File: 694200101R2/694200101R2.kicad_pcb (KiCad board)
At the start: 2 copper layers, 438.6 x 125.8 mm, 402 parts, among them J1 USB4085-GF-A, J2 Conn_01x05_Male, J3 Conn_01x02_Male, SW1 MX_SW, SW10 MX_SW, SW100 MX_SW, SW101 MX_SW, SW102 MX_SW, SW103 MX_SW, SW104 MX_SW, SW105 MX_SW, SW106 MX_SW, SW107 MX_SW, SW11 MX_SW, SW12 MX_SW, SW13 MX_SW, SW14 MX_SW, SW15 MX_SW, SW16 MX_SW, SW17 MX_SW, SW18 MX_SW, SW19 MX_SW, SW2 MX_SW, SW20 MX_SW, SW21 MX_SW, SW22 MX_SW, SW23 MX_SW, SW24 MX_SW, SW25 MX_SW, SW26 MX_SW, SW27 MX_SW, SW28 MX_SW, SW29 MX_SW, SW3 MX_SW, SW30 MX_SW, SW31 MX_SW, SW32 MX_SW, SW33 MX_SW, SW34 MX_SW, SW35 MX_SW, SW36 MX_SW, SW37 MX_SW, SW38 MX_SW, SW39 MX_SW, SW4 MX_SW, SW40 MX_SW, SW41 MX_SW, SW42 MX_SW, SW43 MX_SW, SW44 MX_SW, SW45 MX_SW, SW46 MX_SW, SW47 MX_SW, SW48 MX_SW, SW49 MX_SW, SW5 MX_SW, SW50 MX_SW, SW51 MX_SW, SW52 MX_SW, SW53 MX_SW, SW54 MX_SW, SW55 MX_SW, SW56 MX_SW, SW57 MX_SW, SW58 MX_SW, SW59 MX_SW, SW6 MX_SW, SW60 MX_SW, SW61 MX_SW, SW62 MX_SW, SW63 MX_SW, SW64 MX_SW, SW65 MX_SW, SW66 MX_SW, SW67 MX_SW, SW68 MX_SW, SW69 MX_SW, SW7 MX_SW, SW70 MX_SW, SW71 MX_SW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

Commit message: adjusted led and added pull on program
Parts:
- added R23: RNCP0603FTD10K0, Resistor-Libs:RESC1508X50N, F.Cu at (353.7, 20.6)
- J2: value Conn_01x05_Male -> Conn_01x06_Male; footprint Connector_PinHeader_2.54mm:PinHeader_1x05_P2.54mm_Vertical -> Connector_PinHeader_2.54mm:PinHeader_1x06_P2.54mm_Vertical
- R12, R14: value RNCP0603FTD10K0 -> MCT06030Z0000ZP500; footprint Resistor-Libs:RESC1508X50N -> Resistor-Libs:RESC1508X55N
- moved J2 2.44 mm to (308.5, 29.6)
- moved D217 1.38 mm to (301.3, 72.2)
- turned R12 to 90 degrees
- turned R14 to 90 degrees
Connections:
- J1 pad A8: (no net) -> Net-(J1-PadA8)
- J1 pad B8: (no net) -> Net-(J1-PadB8)
- R12 pad 1: Net-(ENC1-PadA1) -> ENCODER_A
- R12 pad 2: ENCODER_A -> Net-(ENC1-PadA1)
- R14 pad 1: Net-(ENC1-PadB1) -> ENCODER_B
- R14 pad 2: ENCODER_B -> Net-(ENC1-PadB1)
- U3 pad 10: (no net) -> COL_18
- U3 pad 14: (no net) -> Net-(U3-Pad14)
- U3 pad 15: (no net) -> Net-(U3-Pad15)
- U3 pad 16: (no net) -> Net-(U3-Pad16)
- U3 pad 17: (no net) -> Net-(U3-Pad17)
- U3 pad 2: (no net) -> Net-(U3-Pad2)
- U3 pad 3: (no net) -> Net-(U3-Pad3)
- U3 pad 4: (no net) -> Net-(U3-Pad4)
- U3 pad 56: (no net) -> ROW_1
- U3 pad 61: (no net) -> Net-(U3-Pad61)
- U3 pad 62: (no net) -> Net-(U3-Pad62)
- U3 pad 8: (no net) -> Net-(U3-Pad8)
- U5 pad 1: (no net) -> Net-(U5-Pad1)
- U5 pad 36: (no net) -> Net-(U5-Pad36)
- U5 pad 45: (no net) -> Net-(U5-Pad45)
- U6 pad 1: (no net) -> Net-(U6-Pad1)
- U6 pad 30: (no net) -> CS13_B
- U6 pad 31: (no net) -> CS14_B
- U6 pad 32: (no net) -> CS15_B
- U6 pad 33: (no net) -> CS16_B
- U6 pad 36: (no net) -> Net-(U6-Pad36)
- U6 pad 45: (no net) -> Net-(U6-Pad45)
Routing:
- net +3V3: track 803.5 -> 815.8 mm, vias 14 -> 15
- net Net-(J3-Pad2): track 2.42 -> 5.78 mm
- net SWO: track 33.6 -> 36.1 mm
- net SWCLK: track 44.4 -> 46.9 mm
- net /RST: track 49.9 -> 52.3 mm
- net SWDIO: track 40.8 -> 43.0 mm
- net GND: track 626.5 -> 628.8 mm
- net CS12_B: track 252.9 -> 254.3 mm
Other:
- board text added: "694200101R2"
- board text removed: "694200101R1"

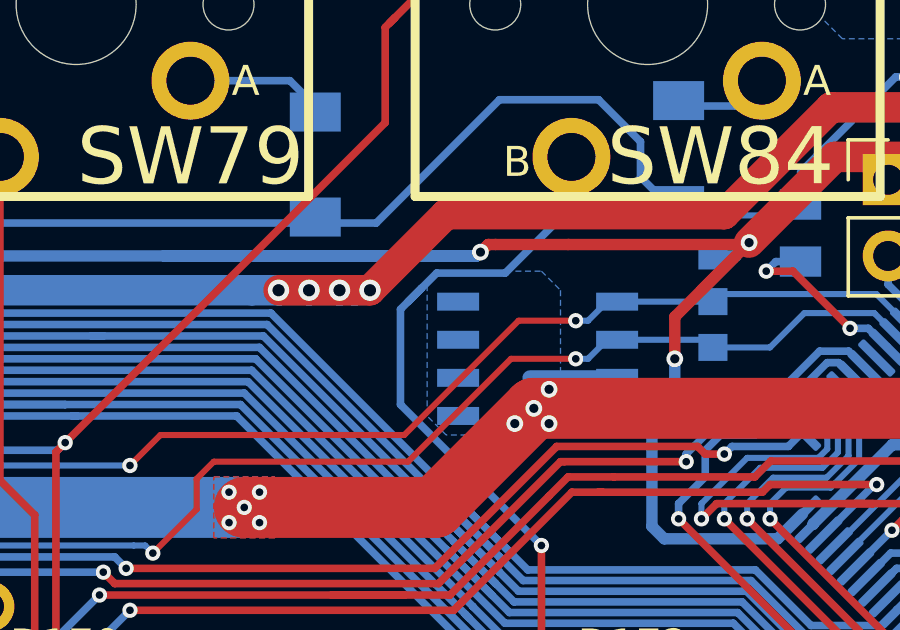
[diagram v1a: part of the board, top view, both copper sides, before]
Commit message: updated eeprom address
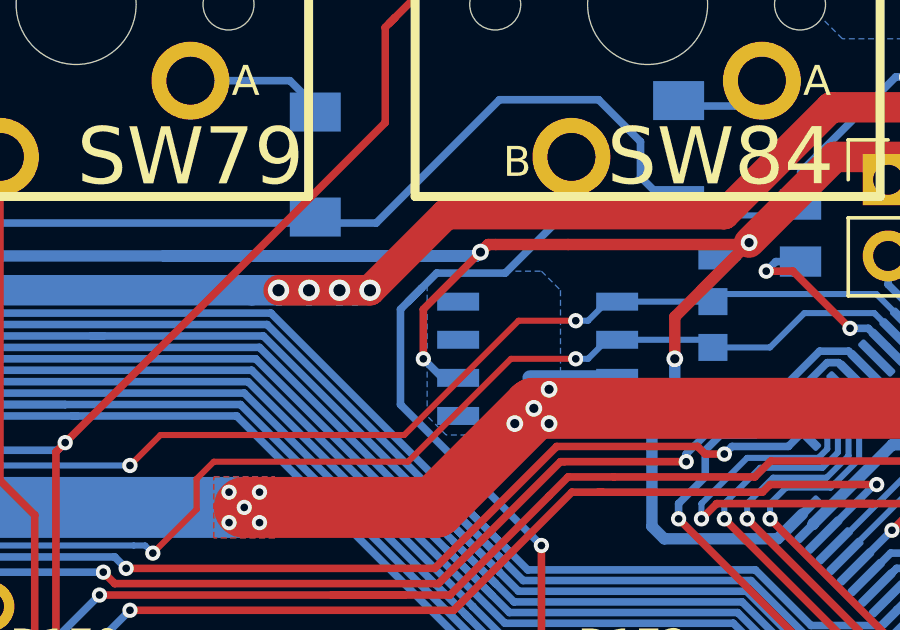
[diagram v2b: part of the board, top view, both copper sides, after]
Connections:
- U4 pad 2: GND -> +3V3
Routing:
- net +3V3: track 815.8 -> 821.5 mm, vias 15 -> 16

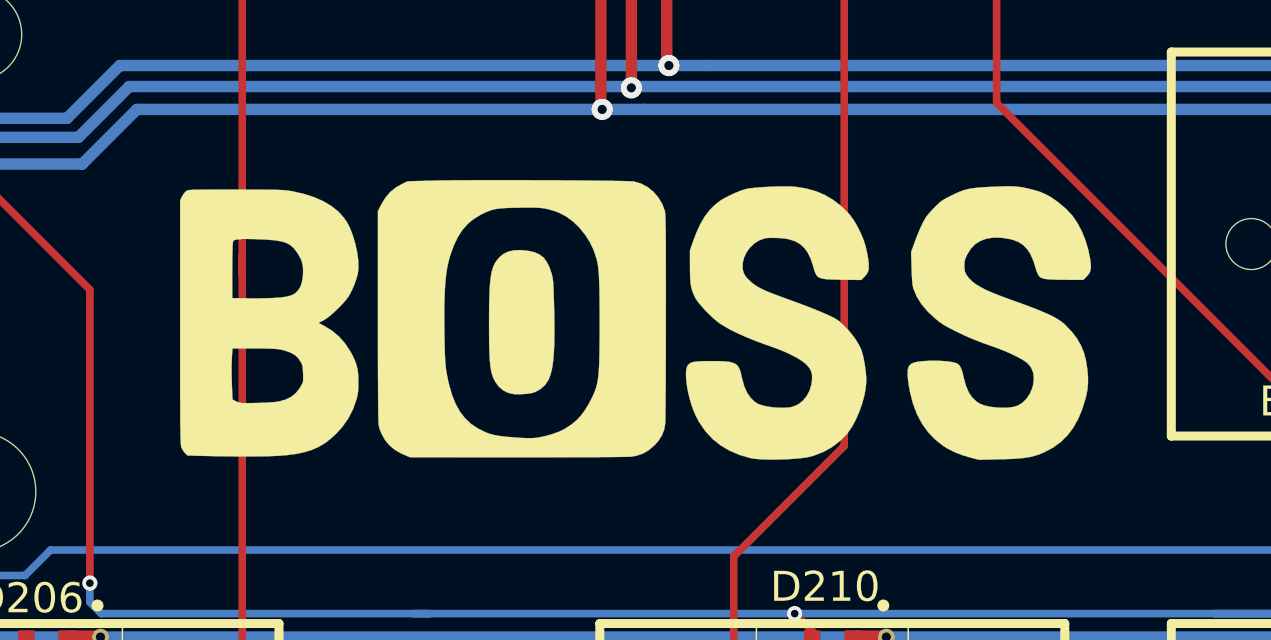
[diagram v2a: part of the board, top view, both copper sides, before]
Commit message: Added Logo and updated USB Connector
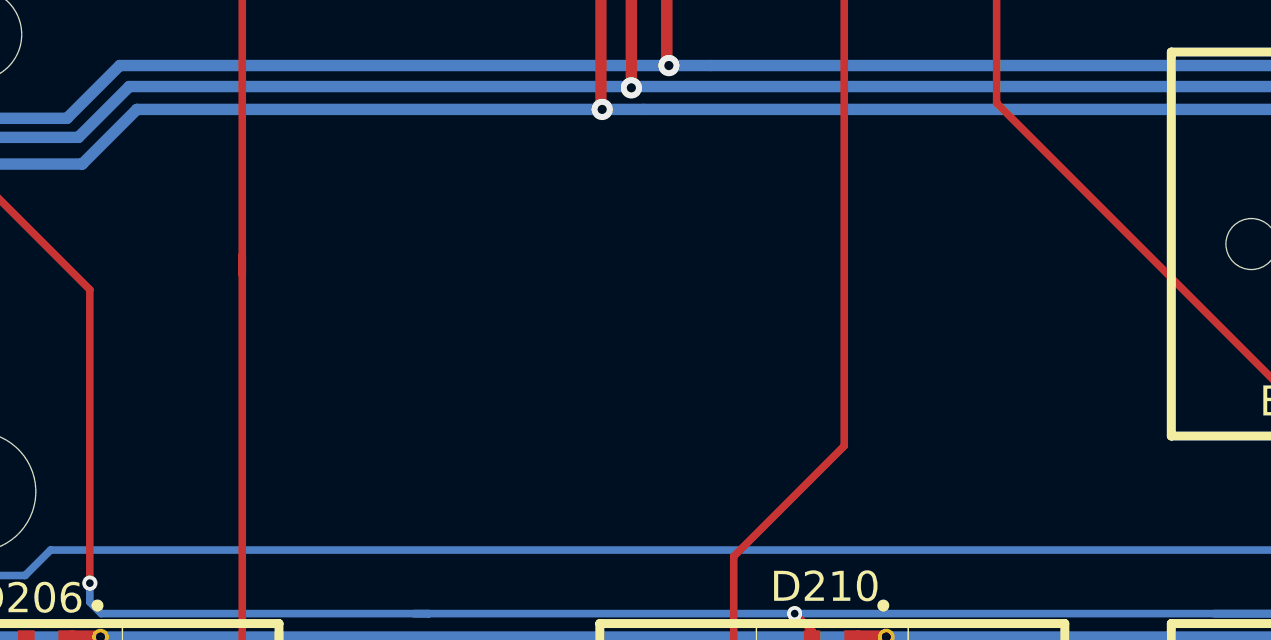
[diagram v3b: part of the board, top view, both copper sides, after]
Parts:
- removed G1: LOGO, BossLogo:BossLogo
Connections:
- U3 pad 10: COL_18 -> (no net)
- U3 pad 14: Net-(U3-Pad14) -> (no net)
- U3 pad 15: Net-(U3-Pad15) -> (no net)
- U3 pad 16: Net-(U3-Pad16) -> (no net)
- U3 pad 17: Net-(U3-Pad17) -> (no net)
- U3 pad 2: Net-(U3-Pad2) -> (no net)
- U3 pad 3: Net-(U3-Pad3) -> (no net)
- U3 pad 4: Net-(U3-Pad4) -> (no net)
- U3 pad 56: ROW_1 -> (no net)
- U3 pad 61: Net-(U3-Pad61) -> (no net)
- U3 pad 62: Net-(U3-Pad62) -> (no net)
- U3 pad 8: Net-(U3-Pad8) -> (no net)

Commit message: Prettied up schematic
Updated Schematic to be more readable and not as crazily wired
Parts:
- J1: value USB4085-GF-A -> USB_C_Receptacle_USB2.0; moved to F.Cu
- U5, U6: footprint cldg:QFN-48_EP_6.6x6.6_Pitch0.4mm -> Package_QFP:TQFP-48-1EP_7x7mm_P0.5mm_EP5x5mm_ThermalVias
- moved J1 9.96 mm to (358.1, -1.91), turned to 180 degrees
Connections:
- net /RST renamed RST
- net Net-(C3-Pad1) renamed OSC_OUT
- net Net-(C6-Pad1) renamed OSC_IN
- net Net-(J3-Pad2) renamed BOOT0
- net Net-(R3-Pad2) renamed ROW_3_MCU
- net Net-(R4-Pad2) renamed ROW_2_MCU
- net Net-(R5-Pad2) renamed ROW_6_MCU
- net Net-(R6-Pad2) renamed ROW_5_MCU
- net Net-(R7-Pad2) renamed ROW_4_MCU
- net Net-(R8-Pad1) renamed ROW_0_MCU
- J1 pad A8: Net-(J1-PadA8) -> (no net)
- J1 pad B8: Net-(J1-PadB8) -> (no net)
- J1 pad S1: (no net) -> Earth
- U5 pad 1: Net-(U5-Pad1) -> (no net)
- U5 pad 36: Net-(U5-Pad36) -> (no net)
- U5 pad 45: Net-(U5-Pad45) -> (no net)
- U6 pad 1: Net-(U6-Pad1) -> (no net)
- U6 pad 30: CS13_B -> (no net)
- U6 pad 31: CS14_B -> (no net)
- U6 pad 32: CS15_B -> (no net)
- U6 pad 33: CS16_B -> (no net)
- U6 pad 36: Net-(U6-Pad36) -> (no net)
- U6 pad 45: Net-(U6-Pad45) -> (no net)

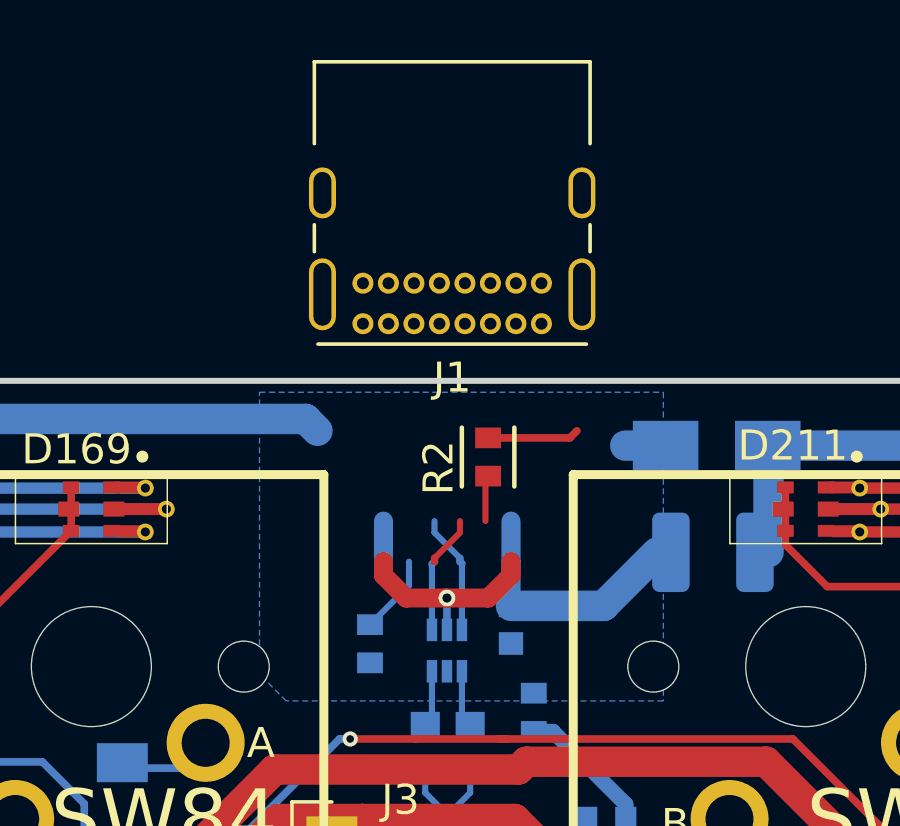
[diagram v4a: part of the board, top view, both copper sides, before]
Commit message: Update 694200101R2.kicad_pcb
Fixed positioning of USB C connector
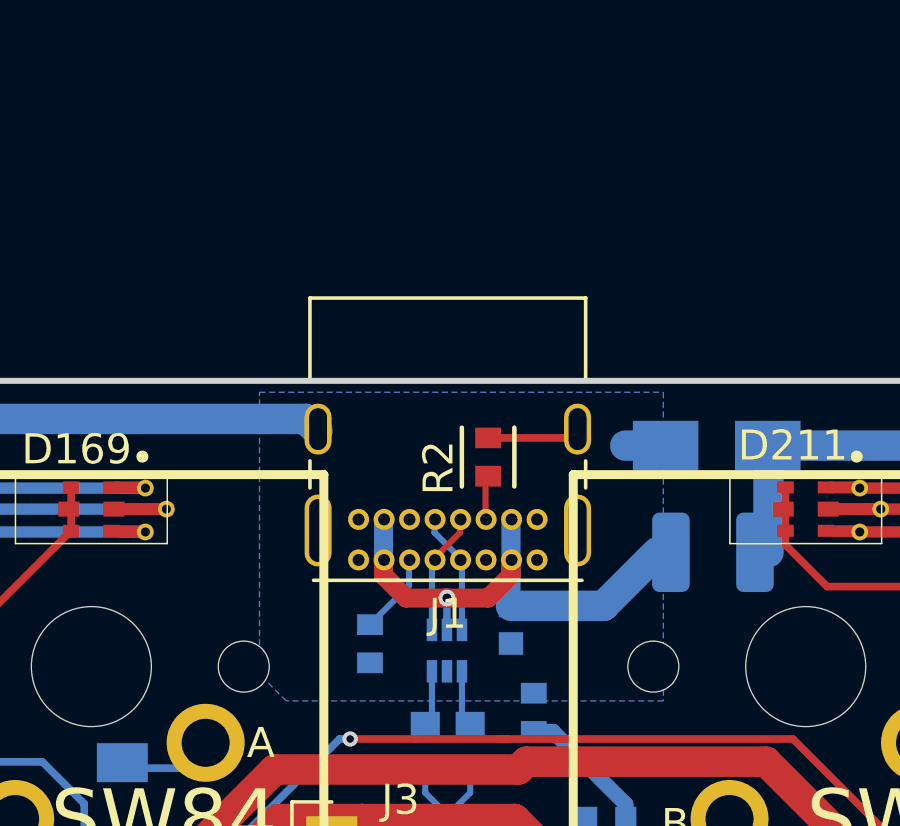
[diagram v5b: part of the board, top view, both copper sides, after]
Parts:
- moved J1 7.88 mm to (358.0, 5.97)

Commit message: working on new led drivers
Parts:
- moved U5 1.66 mm to (29.3, 18.0)
- moved R17 1.27 mm to (38.1, 24.5)
- moved R15 0.51 mm to (26.9, 24.3)
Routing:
- net SW10_A: track 377.8 -> 365.1 mm
- net CS1_A: track 103.8 -> 95.3 mm
- net VCC: track 546.2 -> 538.1 mm
- net I2C_SCL: track 465.7 -> 457.7 mm, vias 6 -> 5
- net SW12_A: track 367.5 -> 359.6 mm
- net GND: track 628.8 -> 621.2 mm, vias 67 -> 60
- net SW9_A: track 356.4 -> 350.5 mm
- net SW8_A: track 364.1 -> 358.4 mm
- net SW7_A: track 353.9 -> 348.4 mm
- net SYNC: track 436.6 -> 431.2 mm, vias 4 -> 3
- net CS2_A: track 135.2 -> 130.1 mm
- net SW6_A: track 390.4 -> 385.4 mm
- net SW5_A: track 398.5 -> 393.7 mm
- net CS4_A: track 163.9 -> 159.2 mm
- net SW11_A: track 383.3 -> 378.9 mm
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
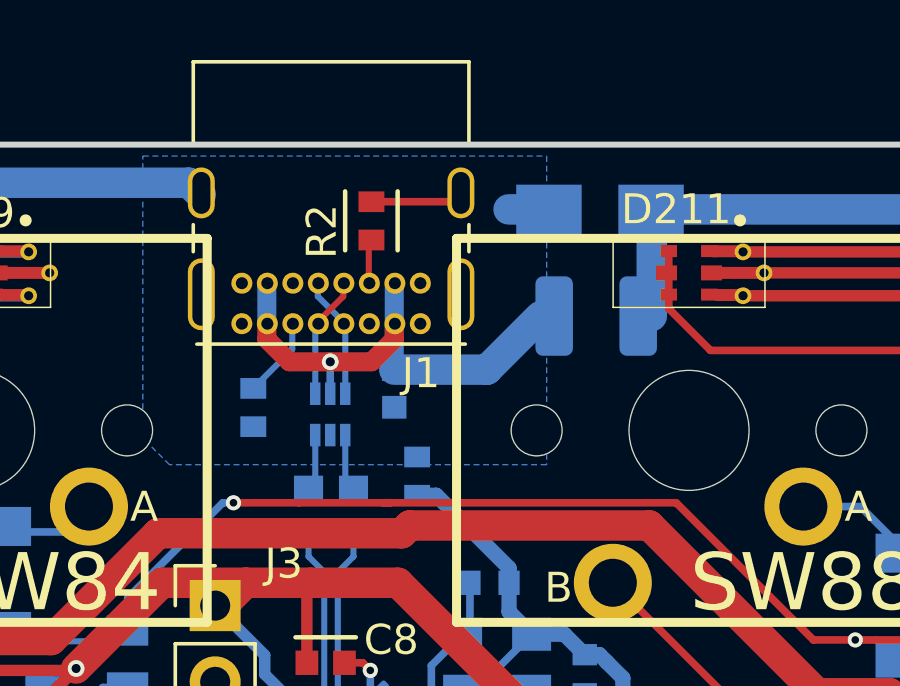
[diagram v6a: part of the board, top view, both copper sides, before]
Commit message: layout to footprint changes
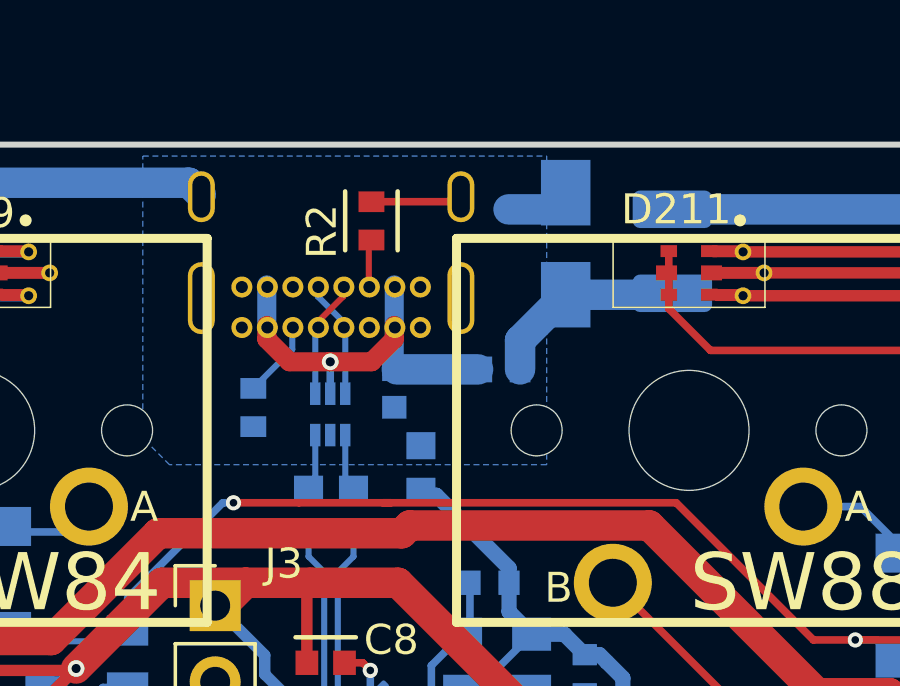
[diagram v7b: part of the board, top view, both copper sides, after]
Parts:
- added R24: MCT06030Z0000ZP500, Resistor-Libs:RESC1508X55N, B.Cu at (358.0, 10.8)
- J1: moved to B.Cu
- moved J1 5.95 mm to (352.0, 6.10), turned to 0 degrees
- moved FB1 4.52 mm to (360.7, 7.49), turned to 180 degrees
- moved F1 3.33 mm to (366.4, 3.56), turned to 90 degrees
- moved CR1 1.62 mm to (362.8, 3.30), turned to 90 degrees
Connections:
- CR1 pad 1: VCC -> Net-(CR1-Pad1)
- F1 pad 1: +5V -> Net-(CR1-Pad1)
- FB1 pad 1: GND -> Net-(CR1-Pad1)
- FB1 pad 2: Earth -> +5V
- J1 pad A8: (no net) -> Net-(J1-PadA8)
- J1 pad B8: (no net) -> Net-(J1-PadB8)
- U3 pad 10: (no net) -> COL_18
- U3 pad 14: (no net) -> Net-(U3-Pad14)
- U3 pad 15: (no net) -> Net-(U3-Pad15)
- U3 pad 16: (no net) -> Net-(U3-Pad16)
- U3 pad 17: (no net) -> Net-(U3-Pad17)
- U3 pad 2: (no net) -> Net-(U3-Pad2)
- U3 pad 3: (no net) -> Net-(U3-Pad3)
- U3 pad 4: (no net) -> Net-(U3-Pad4)
- U3 pad 56: (no net) -> ROW_1
- U3 pad 61: (no net) -> Net-(U3-Pad61)
- U3 pad 62: (no net) -> Net-(U3-Pad62)
- U3 pad 8: (no net) -> Net-(U3-Pad8)
- U5 pad 1: (no net) -> Net-(U5-Pad1)
- U5 pad 36: (no net) -> Net-(U5-Pad36)
- U5 pad 45: (no net) -> Net-(U5-Pad45)
- U6 pad 1: (no net) -> Net-(U6-Pad1)
- U6 pad 30: (no net) -> CS13_B
- U6 pad 31: (no net) -> CS14_B
- U6 pad 32: (no net) -> CS15_B
- U6 pad 33: (no net) -> CS16_B
- U6 pad 36: (no net) -> Net-(U6-Pad36)
- U6 pad 45: (no net) -> Net-(U6-Pad45)
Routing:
- net Net-(CR1-Pad1): track 0.00 -> 6.70 mm
- net VCC: track 538.1 -> 534.6 mm
- net +5V: track 16.6 -> 13.7 mm
